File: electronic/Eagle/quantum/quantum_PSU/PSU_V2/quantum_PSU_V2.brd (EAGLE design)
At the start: 140 x 110 mm, 30 parts, among them J1 90814-0204, J2 90814-0204, J3 PF0030_PC, U1 7815, U2 7812, U4 7805, U5 LD1117AV33

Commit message: PSU_V2 progress...
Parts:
- C1, C3: value (none) -> 4700 uF/25 V
- C10, C12, C4, C5, C6: value (none) -> 100 nF
- C11, C13, C7, C8, C9: value (none) -> 100 uF/25V; device passive components:C5MM -> passive components:ELECTROLYTIC_8MM
- C2: value (none) -> 4700 uF/25V
- U3: value (none) -> 7915
- moved TRANSFORMATOR1 71.8 mm to (62.2, 2.54)
- moved BR1 69.3 mm to (41.9, 55.9)
- moved TRANSFORMATOR2 47.0 mm to (125.7, 6.35)
- moved C3 43.8 mm to (69.8, 82.5), turned to 180 degrees
- moved BR2 43.4 mm to (68.6, 62.2), turned to 90 degrees
- moved C1 21.6 mm to (53.3, 68.6)
- moved C2 21.6 mm to (33.0, 68.6)
- moved C13 12.8 mm to (11.3, 72.4), turned to 180 degrees
- moved D2 11.7 mm to (31.8, 99.1)
- moved C4 11.7 mm to (26.4, 98.4)
- moved U1 11.4 mm to (31.5, 108.4)
- moved C12 11.4 mm to (10.0, 61.0)
- moved C7 10.9 mm to (37.8, 97.2)
- moved C5 6.35 mm to (54.4, 95.1)
- moved D1 5.68 mm to (59.7, 99.1)
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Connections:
- net +12V_OUT: now also C9.+, J2.2; no longer C9.1
- net +15V_OUT: now also C7.+, J1.1; no longer C7.1
- net +3V3_OUT: now also C13.+, J2.1; no longer C13.1
- net +5V_OUT: now also C11.+, J2.4; no longer C11.1
- net -15V_OUT: now also C8.-, J1.2; no longer C8.2
- net AGND: now also C7.-, C8.+, J1.3, J1.4; no longer C7.2, C8.1
- net DGND: now also C11.-, C13.-, C9.-, J2.3; no longer C11.2, C13.2, C9.2
- net N$1: now also TRANSFORMATOR2.P$6; no longer TRANSFORMATOR2.P$5
- net N$3: now also TRANSFORMATOR2.P$5; no longer TRANSFORMATOR2.P$6

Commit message: progress PSU_V2
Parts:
- added BR3: BRIDGE_RECTIFIER, passive components:KBP308G
- added C14, C15, C16, C17, C18: 100 nF, passive components:C5MM
- added X1: (no value), electro_mechanical:W237-103
- moved U3 103.2 mm to (1.02, 23.3), turned to 90 degrees
- moved D1 92.0 mm to (8.89, 22.4), turned to 180 degrees
- moved C5 88.5 mm to (9.91, 18.6), turned to 0 degrees
- moved C8 82.1 mm to (11.3, 35.1)
- moved U1 67.0 mm to (1.02, 48.7), turned to 90 degrees
- moved J3 61.3 mm to (53.3, 116.4)
- moved C3 60.2 mm to (27.9, 125.7), turned to 270 degrees
- moved TRANSFORMATOR2 59.3 mm to (85.1, 49.5)
- moved C4 55.7 mm to (9.91, 45.2), turned to 0 degrees
- moved D2 55.0 mm to (8.89, 49.0), turned to 180 degrees
- moved TRANSFORMATOR1 49.3 mm to (90.2, 43.2), turned to 180 degrees
- moved C2 48.9 mm to (25.4, 20.3)
- moved C7 45.4 mm to (11.2, 60.5)
- moved BR2 43.4 mm to (26.7, 73.7)
- moved C1 41.3 mm to (25.4, 38.1), turned to 180 degrees
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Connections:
- removed net N$1: BR2.2, TRANSFORMATOR2.P$6, TRANSFORMATOR2.P$7
- removed net N$13: BR1.3, TRANSFORMATOR1.P$5
- new net N$4: TRANSFORMATOR1.P$1, TRANSFORMATOR1.P$4
- new net N$5: TRANSFORMATOR2.P$1, TRANSFORMATOR2.P$4
- new net N$6: TRANSFORMATOR2.P$8
- net +12V_OUT: now also C14.1
- net +15V_OUT: now also C18.1
- net +3V3_OUT: now also C16.1
- net +5V_OUT: now also C15.1
- net -15V_OUT: now also C17.2
- net AGND: now also C17.1, C18.2, TRANSFORMATOR1.P$5; no longer TRANSFORMATOR1.P$6
- net CHASSIS: now also X1.3
- net DGND: now also BR3.4, C14.2, C15.2, C16.2
- net N$10: now also BR3.2, TRANSFORMATOR2.P$5; no longer TRANSFORMATOR2.P$2, TRANSFORMATOR2.P$4
- net N$2: now also BR3.1
- net N$3: now also BR1.3, TRANSFORMATOR1.P$6; no longer BR2.3, TRANSFORMATOR2.P$5, TRANSFORMATOR2.P$8
- net N$7: now also BR3.3, TRANSFORMATOR2.P$6; no longer TRANSFORMATOR1.P$2, TRANSFORMATOR1.P$4
- net N$8: now also X1.2
- net N$9: now also TRANSFORMATOR1.P$2, TRANSFORMATOR2.P$2, X1.1; no longer TRANSFORMATOR1.P$1, TRANSFORMATOR2.P$1
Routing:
- net N$8: track 0.00 -> 214.0 mm, vias 0 -> 1
- net N$9: track 0.00 -> 171.1 mm
- net CHASSIS: track 0.00 -> 59.9 mm
- net N$10: track 0.00 -> 55.5 mm
- net N$7: track 0.00 -> 41.2 mm
- net N$4: track 0.00 -> 31.4 mm
- net N$5: track 0.00 -> 29.9 mm
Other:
- board size 140 x 110 mm -> 92.5 x 150 mm

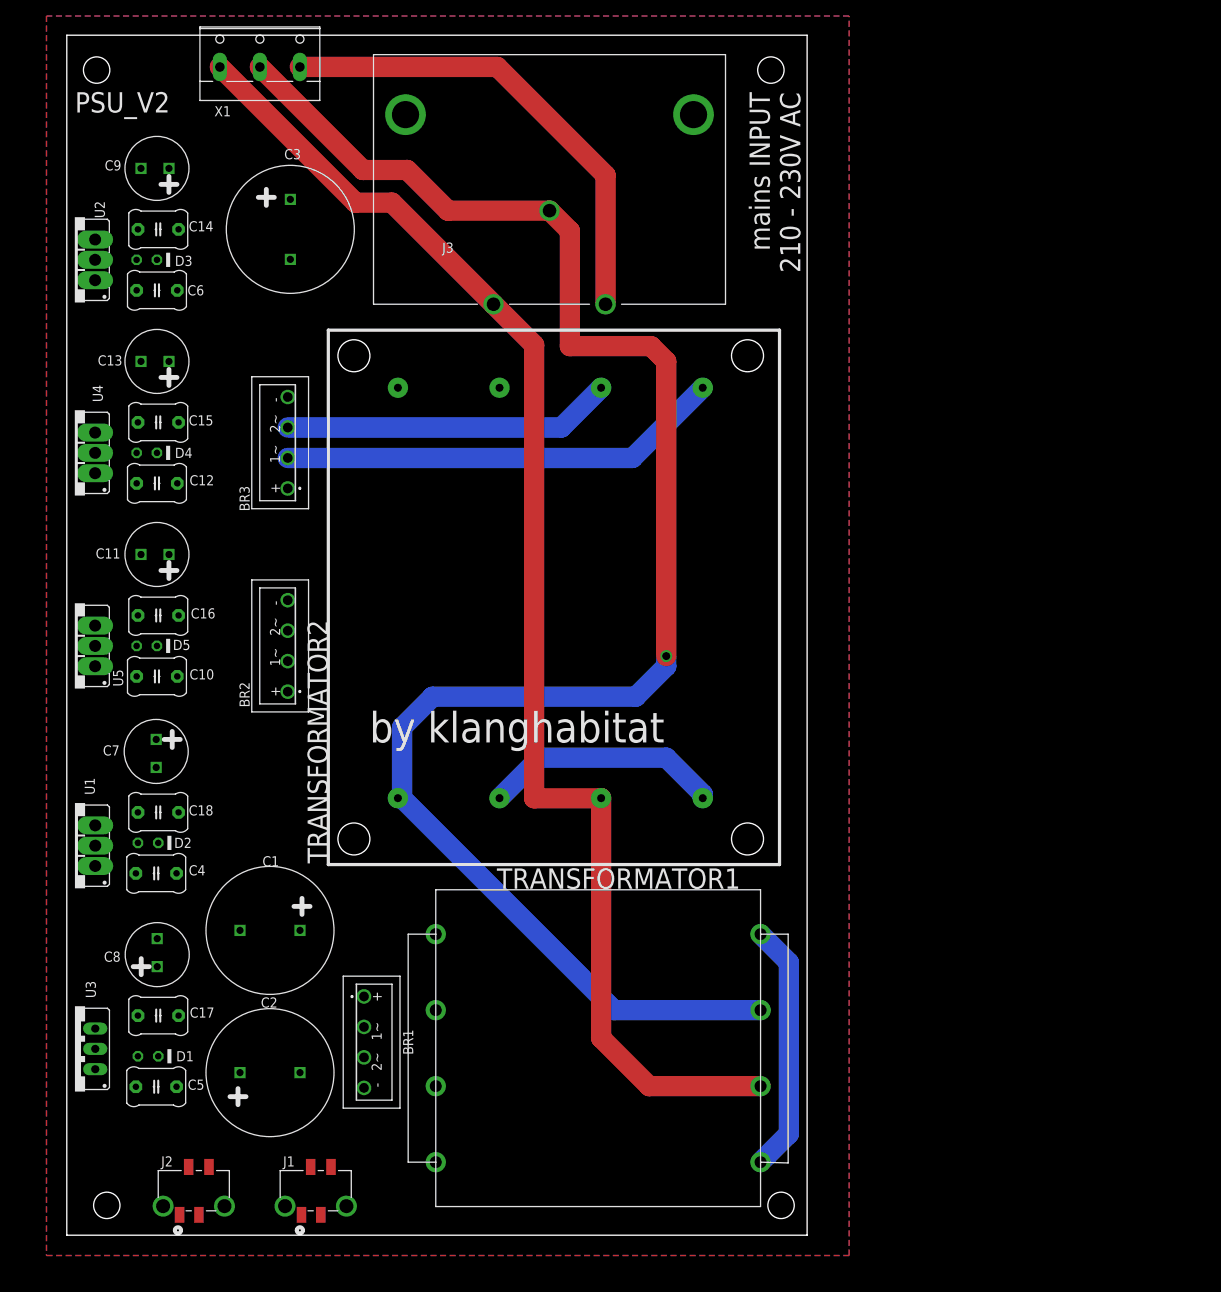
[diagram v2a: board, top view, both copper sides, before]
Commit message: created DiscoveryConnector_V1_0; Finished PSU_V2_0; Changed Light Settings in Encoder
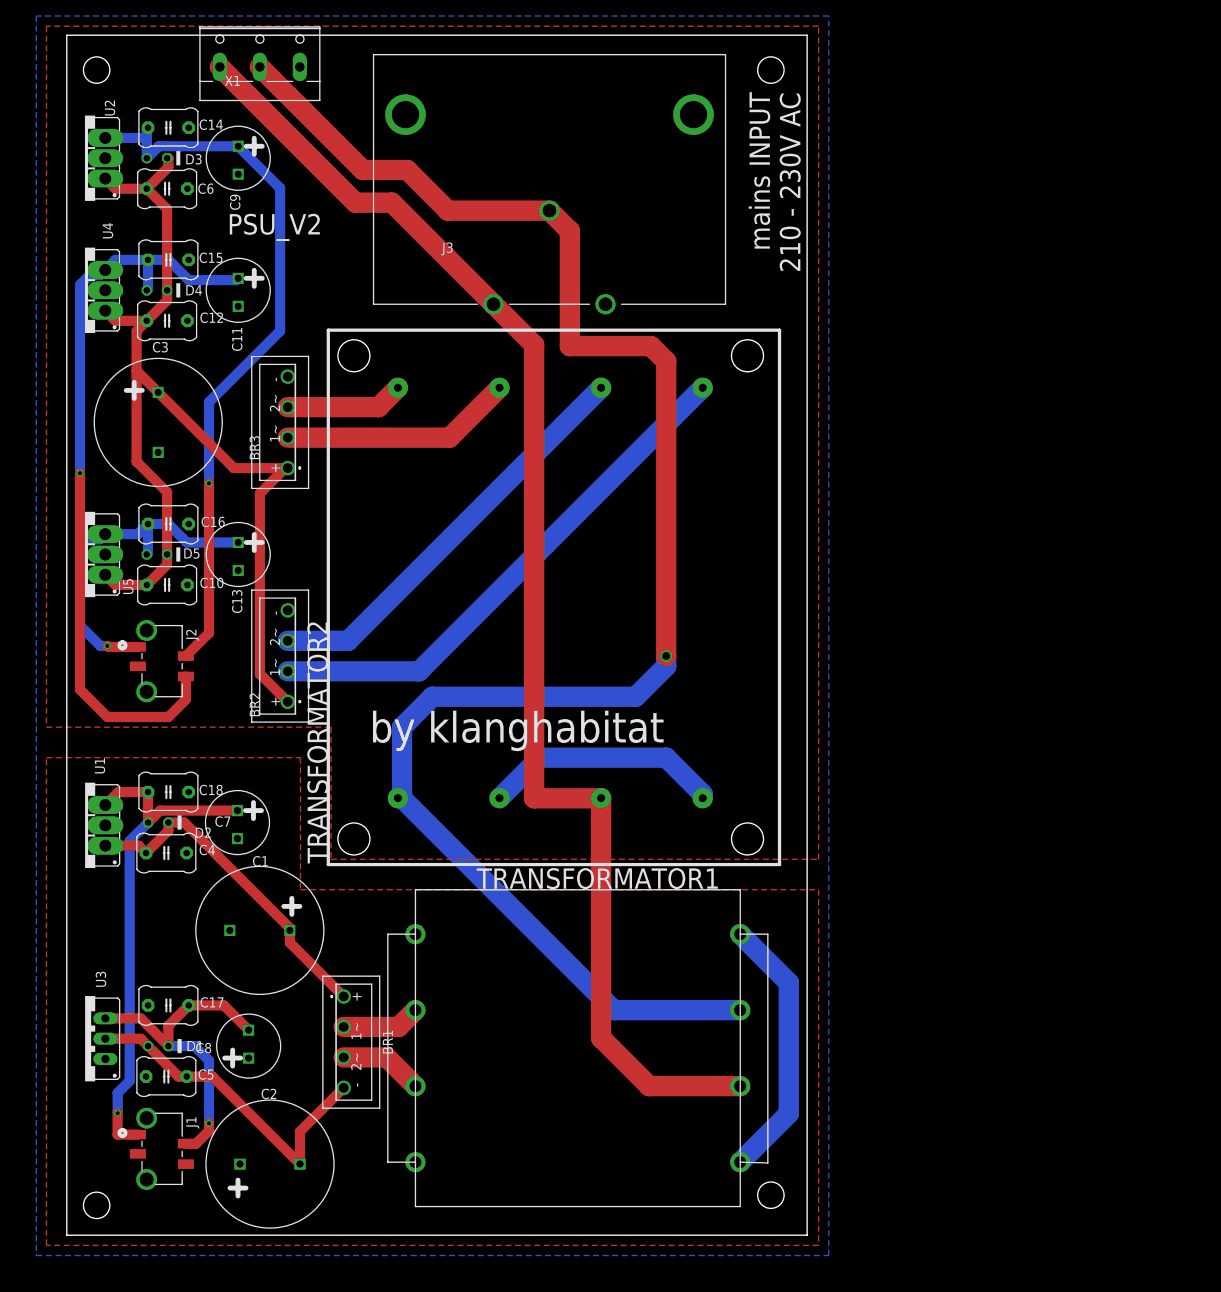
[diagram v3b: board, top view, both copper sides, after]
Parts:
- moved J2 71.3 mm to (8.89, 73.7), turned to 270 degrees
- moved C11 34.5 mm to (21.4, 118.1), turned to 270 degrees
- moved C3 29.2 mm to (11.4, 101.6)
- moved C13 26.2 mm to (21.4, 85.1), turned to 270 degrees
- moved J1 22.7 mm to (8.89, 12.7), turned to 270 degrees
- moved C15 20.4 mm to (11.4, 121.9)
- moved C12 20.4 mm to (11.3, 114.3)
- moved D4 20.4 mm to (10.0, 118.1)
- moved U4 20.4 mm to (2.27, 118.1)
- moved C8 16.2 mm to (22.7, 23.6)
- moved C7 13.5 mm to (21.3, 51.6)
- moved C14 12.8 mm to (11.4, 138.4)
- moved C6 12.8 mm to (11.3, 130.8)
- moved D3 12.8 mm to (10.0, 134.6)
- moved U2 12.8 mm to (2.27, 134.6)
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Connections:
- removed net N$10: BR3.2, TRANSFORMATOR2.P$5
- new net N$1: BR3.3, TRANSFORMATOR2.P$7
- new net N$12: BR2.2, TRANSFORMATOR2.P$5
- net N$6: now also BR3.2
- net N$7: now also BR2.3; no longer BR3.3
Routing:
- net N$2: track 0.00 -> 133.2 mm
- net +5V_OUT: track 0.00 -> 95.1 mm, vias 0 -> 1
- net +12V_OUT: track 0.00 -> 91.9 mm, vias 0 -> 1
- net N$12: track 0.00 -> 66.6 mm
- net +15V_OUT: track 0.00 -> 64.7 mm, vias 0 -> 1
- net CHASSIS: track 59.9 -> 0.00 mm
- net N$10: track 55.5 -> 0.00 mm
- net +3V3_OUT: track 0.00 -> 44.2 mm, vias 0 -> 1
- net N$17: track 0.00 -> 42.6 mm
- net N$15: track 0.00 -> 42.4 mm
- net -15V_OUT: track 0.00 -> 42.4 mm, vias 0 -> 1
- net N$6: track 0.00 -> 29.1 mm
- net N$1: track 0.00 -> 14.8 mm
- net N$7: track 41.2 -> 52.3 mm
- net N$3: track 0.00 -> 10.5 mm
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- added copper zone on layer 1, net AGND
- added copper zone on layer 16, net CHASSIS
- added copper zone on layer 1, net DGND
- removed copper zone on layer 16, net BOTTOM
- removed copper zone on layer 1, net TOP
